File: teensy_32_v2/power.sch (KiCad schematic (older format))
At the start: 0 parts

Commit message: move forward on new hat
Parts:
- added C?: MF-CAP-0805-0.1uF, MF_Passives:MF_Passives-C0805, symbol CAPACITOR_NP_0805
- added J? (x2): 277-1667-ND, Connectors_Phoenix:PhoenixContact_MCV-G_02x5.08mm_Vertical, symbol Conn_01x02_Female
- added Q?: STL62P3LLH6, teensy:POWERFLAT_5x6, symbol Q_PMOS_SGD
- added R?: MF-RES-0805-6.8K, MF_Passives:MF_Passives-R0805, symbol RESISTOR_0805
- added R?: MF-RES-0805-470, MF_Passives:MF_Passives-R0805, symbol RESISTOR_0805
- added R?: MF-RES-0805-220, MF_Passives:MF_Passives-R0805, symbol RESISTOR_0805
- added R?: MF-RES-0805-18K, MF_Passives:MF_Passives-R0805, symbol RESISTOR_0805
- added R?: MF-RES-0805-10K, MF_Passives:MF_Passives-R0805, symbol RESISTOR_0805
- added R?: MF-RES-0805-680K, MF_Passives:MF_Passives-R0805, symbol RESISTOR_0805
- added R?: MF-RES-0805-100K, MF_Passives:MF_Passives-R0805, symbol RESISTOR_0805
- added SWOFF, SWON: MF-SW-TACT-4.2MM, MF_Switches:MF_Switches-TACT4.2MM, symbol TACT_4.2MM
- added U?: MF-DSC-SOT233-BSS138, MF_Discrete_Semiconductor:MF_Discrete_Semiconductor-SOT-23-3, symbol N-CHANNEL_FET_BSS138_SOT-23-3
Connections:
- net labels added: +5V, +BATT, GND, PWR_ON, VSENSE
- wire segments 0 -> 46

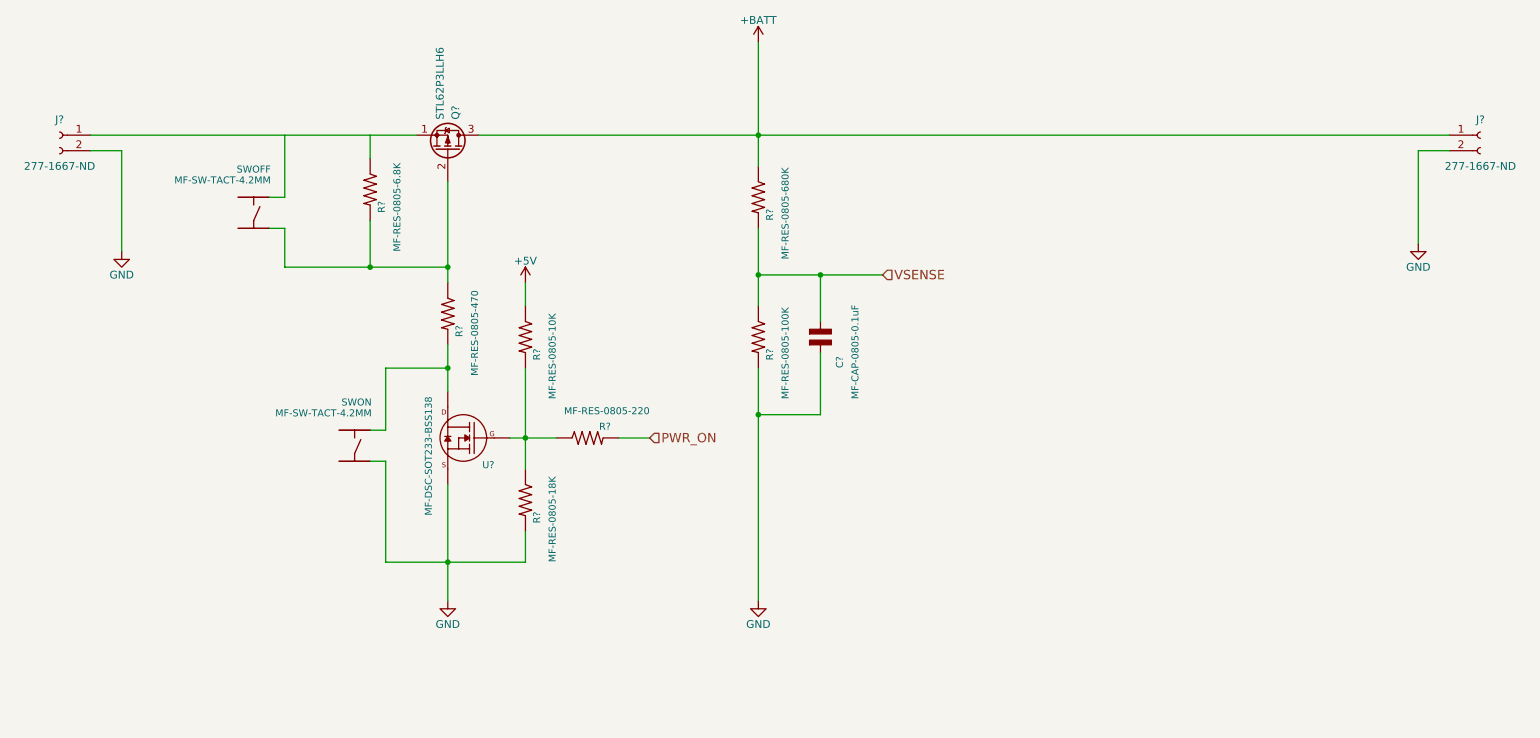
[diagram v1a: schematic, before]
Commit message: power regulator for hat
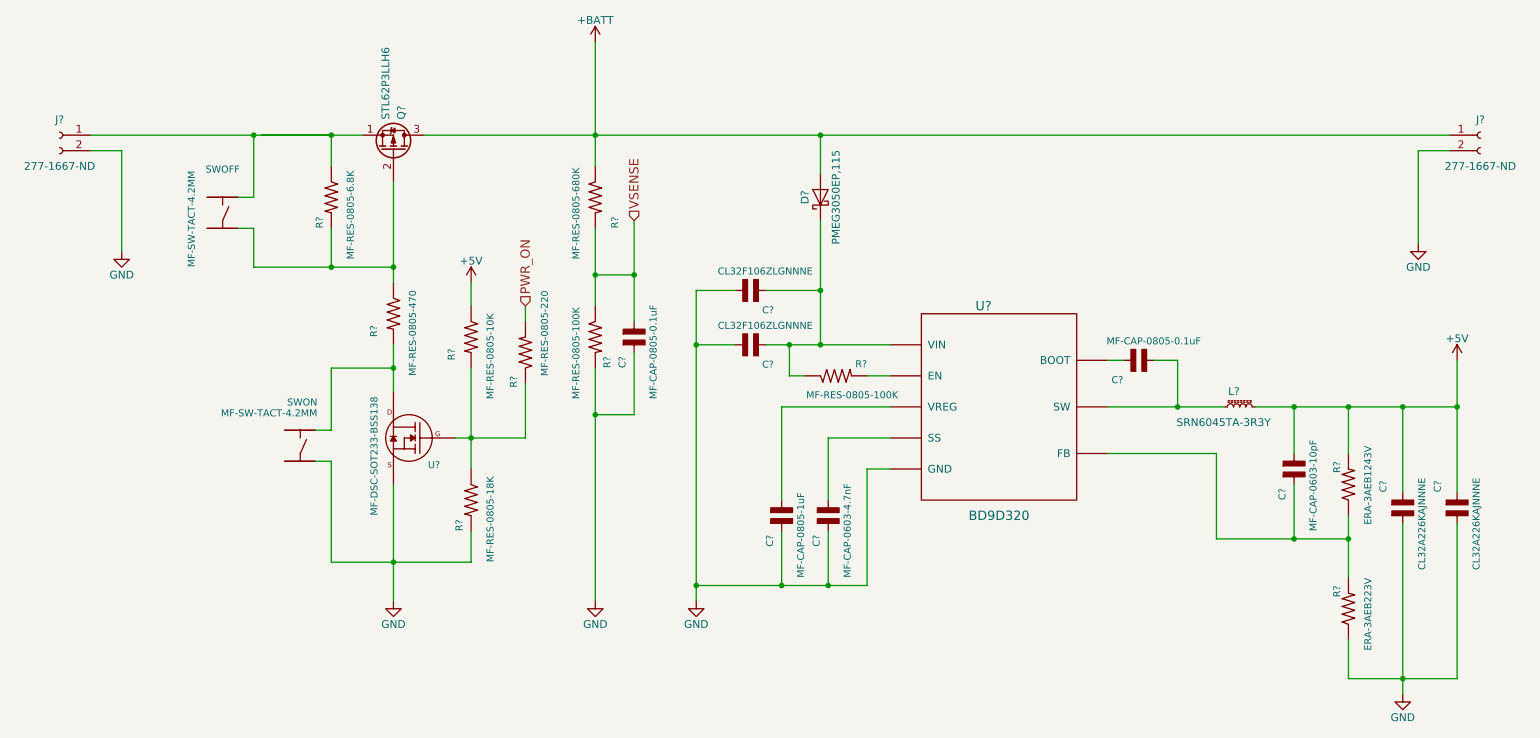
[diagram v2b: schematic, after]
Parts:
- added C?: MF-CAP-0805-0.1uF, MF_Passives:MF_Passives-C0805, symbol CAPACITOR_NP_0805
- added C? (x2): CL32A226KAJNNNE, MF_Passives:MF_Passives-C1210, symbol CAPACITOR_NP_0805
- added C?: MF-CAP-0603-4.7nF, MF_Passives:MF_Passives-C0603, symbol CAPACITOR_NP_0805
- added C?: MF-CAP-0805-1uF, MF_Passives:MF_Passives-C0805, symbol CAPACITOR_NP_0805
- added C? (x2): CL32F106ZLGNNNE, MF_Passives:MF_Passives-C1206, symbol CAPACITOR_NP_0805
- added C?: MF-CAP-0603-10pF, MF_Passives:MF_Passives-C0603, symbol CAPACITOR_NP_0805
- added D?: PMEG3050EP,115, teensy:SOD-128, symbol D_Schottky
- added L?: SRN6045TA-3R3Y, symbol L_Core_Ferrite_Small
- added R?: ERA-3AEB223V, MF_Passives:MF_Passives-R0603, symbol RESISTOR_0805
- added R?: MF-RES-0805-100K, MF_Passives:MF_Passives-R0805, symbol RESISTOR_0805
- added R?: ERA-3AEB1243V, MF_Passives:MF_Passives-R0603, symbol RESISTOR_0805
- added U?: BD9D320, symbol BD9D320
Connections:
- wire segments 46 -> 104
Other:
- moved on the sheet: C?, Q?, R?, SWOFF, SWON, U?

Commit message: schematic tweaks
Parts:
- added C?: MF-CAP-0805-0.1uF, MF_Passives:MF_Passives-C0805, symbol CAPACITOR_NP_0805
- R?: value MF-RES-0805-220 -> MF-RES-0805-470
- R?: value MF-RES-0805-18K -> MF-RES-0805-220K
- R?: value MF-RES-0805-10K -> MF-RES-0805-100K
- R?: value MF-RES-0805-680K -> MF-RES-0805-470K
- R?: value MF-RES-0805-100K -> MF-RES-0805-680K
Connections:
- net GND: now also C?.1
- net at C?.2, C?.2, D?.1 (K)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: now also C?.2

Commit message: more hat
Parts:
- removed U?: BD9D320, symbol BD9D320
- L1: renamed from L?; footprint (none) -> teensy:SRN6045TA
- gave numbers to parts that had none: 25
- renumbered SWOFF to SWOFF1, SWON to SWON1
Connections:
- wire segments 75 -> 77
- no-connect marks 0 -> 4
